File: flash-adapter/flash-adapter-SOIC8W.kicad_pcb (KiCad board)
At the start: 2 copper layers, 10 x 8.5 mm, 3 parts, among them J101 Conn_02x04_Odd_Even, U101 W25Q64FVSS

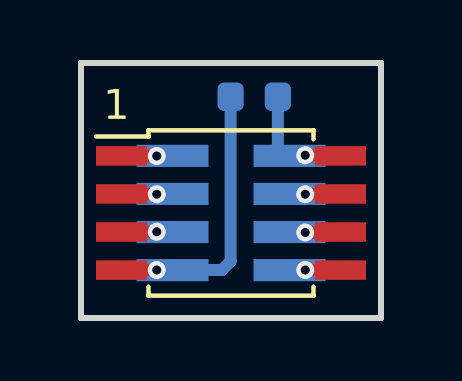
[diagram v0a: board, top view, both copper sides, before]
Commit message: flash-adapter-SOIC8W: move vias from underneath the chip
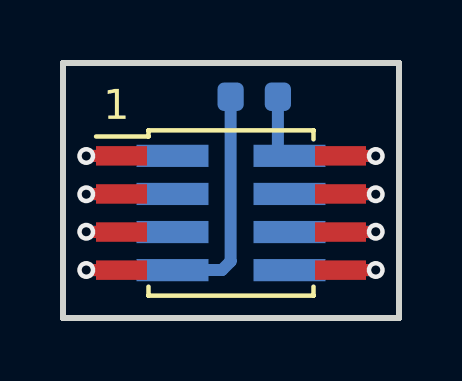
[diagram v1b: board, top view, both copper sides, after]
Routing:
- net /~WP: track 1.18 -> 4.06 mm
- net /~HOLD: track 1.18 -> 4.06 mm
- net /DQ1: track 1.18 -> 4.06 mm
- net /CLK: track 1.18 -> 4.06 mm
- net /~CS: track 1.18 -> 4.05 mm
- net /DQ0: track 1.18 -> 4.05 mm
- net /VCC: track 3.20 -> 6.08 mm
- net /GND: track 9.25 -> 11.7 mm
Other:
- board size 10 x 8.5 mm -> 11.2 x 8.5 mm
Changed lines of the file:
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@@
     (thickness 1.6)
     (drawings 5)
-    (tracks 38)
+    (tracks 45)
     (zones 0)
     (modules 3)
@@
     (effects (font (size 1 1) (thickness 0.25)))
   )
-  (gr_line (start 95 103.5) (end 95 95) (layer Edge.Cuts) (width 0.2))
-  (gr_line (start 105 103.5) (end 95 103.5) (layer Edge.Cuts) (width 0.2))
-  (gr_line (start 105 95) (end 105 103.5) (layer Edge.Cuts) (width 0.2))
-  (gr_line (start 95 95) (end 105 95) (layer Edge.Cuts) (width 0.2))
-  (segment (start 97.100736 98.1) (end 97.525 98.1) (width 0.4) (layer F.Cu) (net 1))
-  (segment (start 96.35 98.095) (end 96.355 98.1) (width 0.4) (layer F.Cu) (net 1))
-  (segment (start 96.355 98.1) (end 97.100736 98.1) (width 0.4) (layer F.Cu) (net 1))
-  (via (at 97.525 98.1) (size 0.6) (drill 0.3) (layers F.Cu B.Cu) (net 1))
-  (segment (start 97.100736 99.375) (end 97.525 99.375) (width 0.4) (layer F.Cu) (net 2))
-  (segment (start 96.36 99.375) (end 97.100736 99.375) (width 0.4) (layer F.Cu) (net 2))
-  (segment (start 96.35 99.365) (end 96.36 99.375) (width 0.4) (layer F.Cu) (net 2))
-  (via (at 97.525 99.375) (size 0.6) (drill 0.3) (layers F.Cu B.Cu) (net 2))
-  (via (at 97.525 100.625) (size 0.6) (drill 0.3) (layers F.Cu B.Cu) (net 3))
-  (segment (start 96.36 100.625) (end 97.100736 100.625) (width 0.4) (layer F.Cu) (net 3))
-  (segment (start 96.35 100.635) (end 96.36 100.625) (width 0.4) (layer F.Cu) (net 3))
-  (segment (start 97.100736 100.625) (end 97.525 100.625) (width 0.4) (layer F.Cu) (net 3))
-  (segment (start 96.35 101.905) (end 96.355 101.9) (width 0.4) (layer F.Cu) (net 4))
+  (gr_line (start 94.4 103.5) (end 94.4 95) (layer Edge.Cuts) (width 0.2))
+  (gr_line (start 105.6 103.5) (end 94.4 103.5) (layer Edge.Cuts) (width 0.2))
+  (gr_line (start 105.6 95) (end 105.6 103.5) (layer Edge.Cuts) (width 0.2))
+  (gr_line (start 94.4 95) (end 105.6 95) (layer Edge.Cuts) (width 0.2))
+  (via (at 95.175 98.1) (size 0.6) (drill 0.3) (layers F.Cu B.Cu) (net 1))
+  (segment (start 95.18 98.095) (end 95.175 98.1) (width 0.4) (layer F.Cu) (net 1))
+  (segment (start 96.35 98.095) (end 95.18 98.095) (width 0.4) (layer F.Cu) (net 1))
+  (segment (start 98.045 98.1) (end 98.05 98.095) (width 0.4) (layer B.Cu) (net 1))
+  (segment (start 95.175 98.1) (end 98.045 98.1) (width 0.4) (layer B.Cu) (net 1))
+  (via (at 95.175 99.375) (size 0.6) (drill 0.3) (layers F.Cu B.Cu) (net 2))
+  (segment (start 95.185 99.365) (end 95.175 99.375) (width 0.4) (layer F.Cu) (net 2))
+  (segment (start 96.35 99.365) (end 95.185 99.365) (width 0.4) (layer F.Cu) (net 2))
+  (segment (start 98.04 99.375) (end 98.05 99.365) (width 0.4) (layer B.Cu) (net 2))
+  (segment (start 95.175 99.375) (end 98.04 99.375) (width 0.4) (layer B.Cu) (net 2))
+  (via (at 95.175 100.625) (size 0.6) (drill 0.3) (layers F.Cu B.Cu) (net 3))
+  (segment (start 95.185 100.635) (end 95.175 100.625) (width 0.4) (layer F.Cu) (net 3))
+  (segment (start 96.35 100.635) (end 95.185 100.635) (width 0.4) (layer F.Cu) (net 3))
+  (segment (start 98.04 100.625) (end 98.05 100.635) (width 0.4) (layer B.Cu) (net 3))
+  (segment (start 95.175 100.625) (end 98.04 100.625) (width 0.4) (layer B.Cu) (net 3))
   (segment (start 99.9875 101.6125) (end 99.7 101.9) (width 0.4) (layer B.Cu) (net 4))
   (segment (start 99.7 101.9) (end 97.949264 101.9) (width 0.4) (layer B.Cu) (net 4))
-  (via (at 97.525 101.9) (size 0.6) (drill 0.3) (layers F.Cu B.Cu) (net 4))
-  (segment (start 97.100736 101.9) (end 97.525 101.9) (width 0.4) (layer F.Cu) (net 4))
-  (segment (start 96.355 101.9) (end 97.100736 101.9) (width 0.4) (layer F.Cu) (net 4))
   (segment (start 99.9875 96.125) (end 99.9875 101.6125) (width 0.4) (layer B.Cu) (net 4))
-  (segment (start 97.949264 101.9) (end 97.525 101.9) (width 0.4) (layer B.Cu) (net 4))
-  (via (at 102.475 101.899994) (size 0.6) (drill 0.3) (layers F.Cu B.Cu) (net 5))
-  (segment (start 103.65 101.905) (end 103.644994 101.899994) (width 0.4) (layer F.Cu) (net 5))
-  (segment (start 103.644994 101.899994) (end 102.899264 101.899994) (width 0.4) (layer F.Cu) (net 5))
-  (segment (start 102.899264 101.899994) (end 102.475 101.899994) (width 0.4) (layer F.Cu) (net 5))
-  (segment (start 102.899264 100.65) (end 102.475 100.65) (width 0.4) (layer F.Cu) (net 6))
-  (segment (start 103.635 100.65) (end 102.899264 100.65) (width 0.4) (layer F.Cu) (net 6))
-  (segment (start 103.65 100.635) (end 103.635 100.65) (width 0.4) (layer F.Cu) (net 6))
-  (via (at 102.475 100.65) (size 0.6) (drill 0.3) (layers F.Cu B.Cu) (net 6))
-  (segment (start 102.899264 99.375) (end 102.475 99.375) (width 0.4) (layer F.Cu) (net 7))
-  (segment (start 103.65 99.365) (end 103.64 99.375) (width 0.4) (layer F.Cu) (net 7))
-  (segment (start 103.64 99.375) (end 102.899264 99.375) (width 0.4) (layer F.Cu) (net 7))
-  (via (at 102.475 99.375) (size 0.6) (drill 0.3) (layers F.Cu B.Cu) (net 7))
-  (segment (start 102.899264 98.075) (end 102.475 98.075) (width 0.4) (layer F.Cu) (net 8))
-  (segment (start 103.63 98.075) (end 102.899264 98.075) (width 0.4) (layer F.Cu) (net 8))
-  (segment (start 103.65 98.095) (end 103.63 98.075) (width 0.4) (layer F.Cu) (net 8))
-  (via (at 102.475 98.075) (size 0.6) (drill 0.3) (layers F.Cu B.Cu) (net 8))
+  (via (at 95.175 101.9) (size 0.6) (drill 0.3) (layers F.Cu B.Cu) (net 4))
+  (segment (start 95.18 101.905) (end 95.175 101.9) (width 0.4) (layer F.Cu) (net 4))
+  (segment (start 96.35 101.905) (end 95.18 101.905) (width 0.4) (layer F.Cu) (net 4))
+  (segment (start 98.045 101.9) (end 98.05 101.905) (width 0.4) (layer B.Cu) (net 4))
+  (segment (start 95.175 101.9) (end 98.045 101.9) (width 0.4) (layer B.Cu) (net 4))
+  (via (at 104.825 101.9) (size 0.6) (drill 0.3) (layers F.Cu B.Cu) (net 5))
+  (segment (start 104.82 101.905) (end 104.825 101.9) (width 0.4) (layer F.Cu) (net 5))
+  (segment (start 103.65 101.905) (end 104.82 101.905) (width 0.4) (layer F.Cu) (net 5))
+  (segment (start 101.955 101.9) (end 101.95 101.905) (width 0.4) (layer B.Cu) (net 5))
+  (segment (start 104.825 101.9) (end 101.955 101.9) (width 0.4) (layer B.Cu) (net 5))
+  (via (at 104.825 100.625) (size 0.6) (drill 0.3) (layers F.Cu B.Cu) (net 6))
+  (segment (start 104.815 100.635) (end 104.825 100.625) (width 0.4) (layer F.Cu) (net 6))
+  (segment (start 103.65 100.635) (end 104.815 100.635) (width 0.4) (layer F.Cu) (net 6))
+  (segment (start 101.96 100.625) (end 101.95 100.635) (width 0.4) (layer B.Cu) (net 6))
+  (segment (start 104.825 100.625) (end 101.96 100.625) (width 0.4) (layer B.Cu) (net 6))
+  (via (at 104.825 99.375) (size 0.6) (drill 0.3) (layers F.Cu B.Cu) (net 7))
+  (segment (start 104.815 99.365) (end 104.825 99.375) (width 0.4) (layer F.Cu) (net 7))
+  (segment (start 103.65 99.365) (end 104.815 99.365) (width 0.4) (layer F.Cu) (net 7))
+  (segment (start 101.96 99.375) (end 101.95 99.365) (width 0.4) (layer B.Cu) (net 7))
+  (segment (start 104.825 99.375) (end 101.96 99.375) (width 0.4) (layer B.Cu) (net 7))
   (segment (start 101.5625 97.9875) (end 101.675 98.1) (width 0.4) (layer B.Cu) (net 8))
   (segment (start 101.5625 96.125) (end 101.5625 97.9875) (width 0.4) (layer B.Cu) (net 8))
+  (via (at 104.825 98.1) (size 0.6) (drill 0.3) (layers F.Cu B.Cu) (net 8))
+  (segment (start 104.82 98.095) (end 104.825 98.1) (width 0.4) (layer F.Cu) (net 8))
+  (segment (start 103.65 98.095) (end 104.82 98.095) (width 0.4) (layer F.Cu) (net 8))
+  (segment (start 101.955 98.1) (end 101.95 98.095) (width 0.4) (layer B.Cu) (net 8))
+  (segment (start 104.825 98.1) (end 101.955 98.1) (width 0.4) (layer B.Cu) (net 8))
 )
